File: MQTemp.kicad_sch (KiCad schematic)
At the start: 8 parts, among them J1 Conn_01x02_Male, SW1 SW_DIP_x01

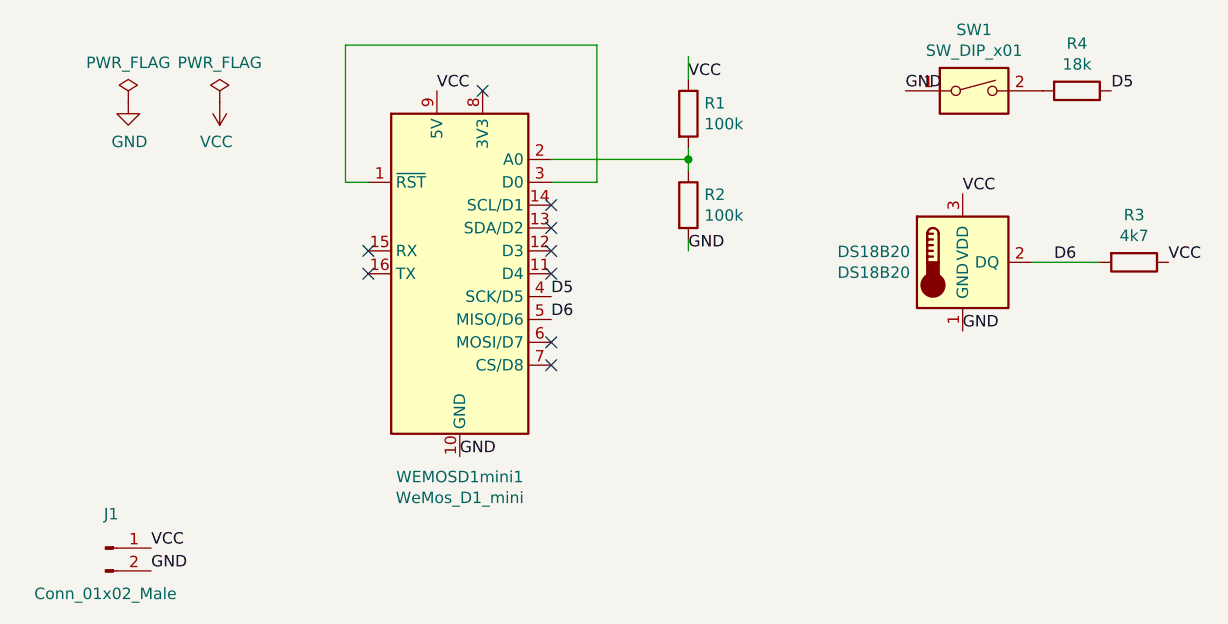
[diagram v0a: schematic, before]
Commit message: Changed input voltage to 3.3V
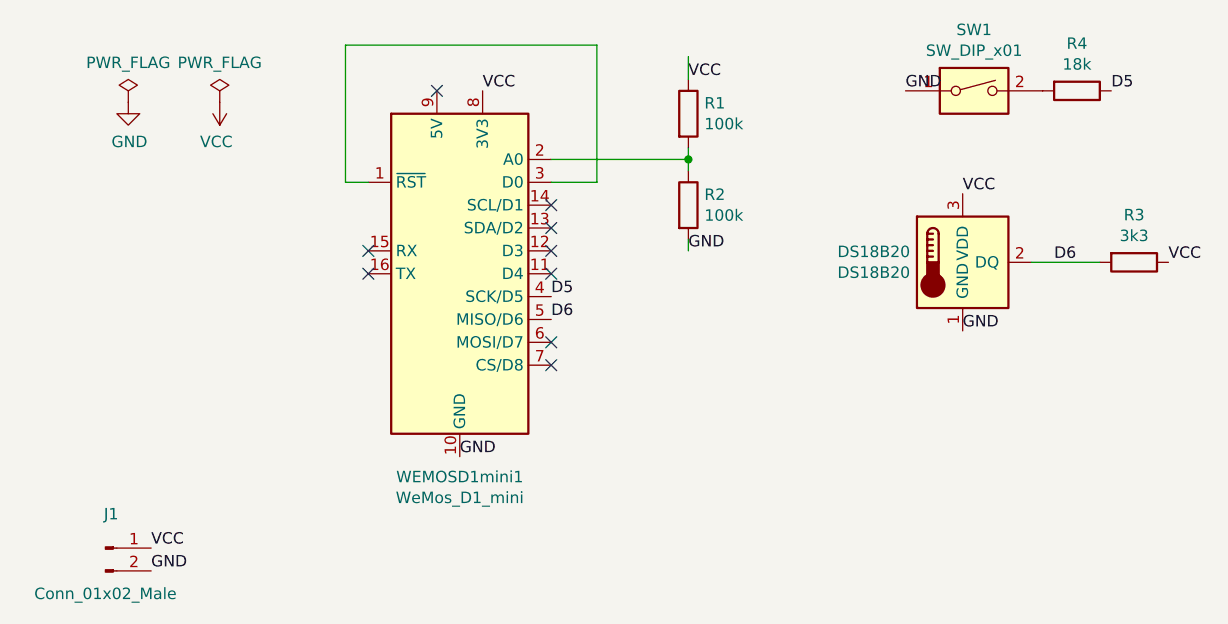
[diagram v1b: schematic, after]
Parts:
- R3: value 4k7 -> 3k3
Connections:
- net VCC: now also WEMOSD1mini1.8 (3V3); no longer WEMOSD1mini1.9 (5V)
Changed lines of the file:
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@@
   (no_connect (at 72.39 53.34))
   (no_connect (at 52.07 43.18))
+  (no_connect (at 59.69 22.86))
   (no_connect (at 72.39 43.18))
   (no_connect (at 72.39 35.56))
   (no_connect (at 72.39 38.1))
   (no_connect (at 52.07 40.64))
-  (no_connect (at 64.77 22.86))
   (no_connect (at 72.39 50.8))
   (no_connect (at 72.39 40.64))
@@
     (effects (font (size 1.27 1.27)) (justify left bottom))
   )
-  (label "VCC" (at 59.69 22.86 0)
+  (label "VCC" (at 64.77 22.86 0)
     (effects (font (size 1.27 1.27)) (justify left bottom))
   )
@@
     (in_bom yes) (on_board yes)
     (property "Reference" "R3" (id 0) (at 137.16 36.6522 90))
-    (property "Value" "4k7" (id 1) (at 137.16 38.9636 90))
+    (property "Value" "3k3" (id 1) (at 137.16 38.9636 90))
     (property "Footprint" "Resistor_THT:R_Axial_DIN0207_L6.3mm_D2.5mm_P10.16mm_Horizontal" (id 2) (at 137.16 40.132 90)
       (effects (font (size 1.27 1.27)) hide)
@@
     )
     (path "/00000000-0000-0000-0000-000062f50d76"
-      (reference "R3") (unit 1) (value "4k7") (footprint "Resistor_THT:R_Axial_DIN0207_L6.3mm_D2.5mm_P10.16mm_Horizontal")
+      (reference "R3") (unit 1) (value "3k3") (footprint "Resistor_THT:R_Axial_DIN0207_L6.3mm_D2.5mm_P10.16mm_Horizontal")
     )
     (path "/00000000-0000-0000-0000-000062f51351"
